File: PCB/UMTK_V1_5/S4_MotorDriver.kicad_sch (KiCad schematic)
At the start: 0 parts

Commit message: Put in Files for V1
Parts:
- added C1: CAP 1uF 6.3V 1206(3216), CAPC1206(3216)130_M, symbol UMTK-altium-import:root_1_CAP_0
- added C2: CAP 1uF 25V 1206(3216), CAPC1206(3216)130_M, symbol UMTK-altium-import:root_0_CAP_0
- added C3: CAP 47nF 50V 1206(3216), CAPC1206(3216)130_L, symbol UMTK-altium-import:root_1_CAP_0
- added C4: 0.1u, Ceramic Cap 5mm, symbol UMTK-altium-import:root_0_Cap
- added J2: Motor Out, symbol Connector:Screw_Terminal_01x02
- added J3: Motor Shunt, symbol Connector:Screw_Terminal_01x02
- added R25: Res1, AXIAL-0.3-3D, symbol UMTK-altium-import:root_0_Res1
- added R26, R27, R32: Res1, AXIAL-0.3-3D, symbol UMTK-altium-import:root_2_Res1
- added R28, R29, R30: Res1, AXIAL-0.3-3D, symbol UMTK-altium-import:root_1_Res1
- added R31: Res1, AXIAL-0.3-3D, symbol UMTK-altium-import:root_3_Res1
- added X3: DRV8873H, DRV8873, symbol UMTK-altium-import:root_0_DRV8873
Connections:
- new net: R31.1, R32.2, X3.10 (IPROPI1), X3.12 (IPROPI2)
- new net: R26.1, R27.1, X3.4 (SR)
- new net: C1.2, X3.1 (DVDD)
- new net: C2.2, X3.21 (VCP)
- new net: C3.1, X3.23 (CPL)
- new net: C3.2, X3.22 (CPH)
- new net +12V: J3.1 (Pin_1)
- new net +5: R25.1, R26.2, R28.2, R29.2, R30.2, X3.3 (MODE)
- new net GND: C1.1, C4.2, R27.2, R31.2, X3.16 (SRC), X3.17 (SRC), X3.24 (GND), X3.25 (PPAD)
- new net M_DISABLE: R30.1, X3.2 (nFAULT)
- new net M_EN/IN1: X3.7 (EN/IN1)
- new net M_FAULT: X3.9 (DISABLE)
- new net M_ISENS: C4.1, R32.1
- new net M_ITRIP: R29.1, X3.5 (nITRIP)
- new net M_OL: R28.1, X3.6 (nOL)
- new net M_PH/IN2: X3.8 (PH/IN2)
- new net M_SLEEP: R25.2, X3.11 (nSLEEP)
- new net VM+: J2.2 (Pin_2), X3.18 (OUT2), X3.19 (OUT1)
- new net VM-: J2.1 (Pin_1), X3.14 (OUT2), X3.15 (OUT2)
- new net Vmot: C2.1, X3.13 (VM), X3.20 (VM)
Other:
- note added: "Motor Connections"
- note added: "Motor Driver (DRV8873)"

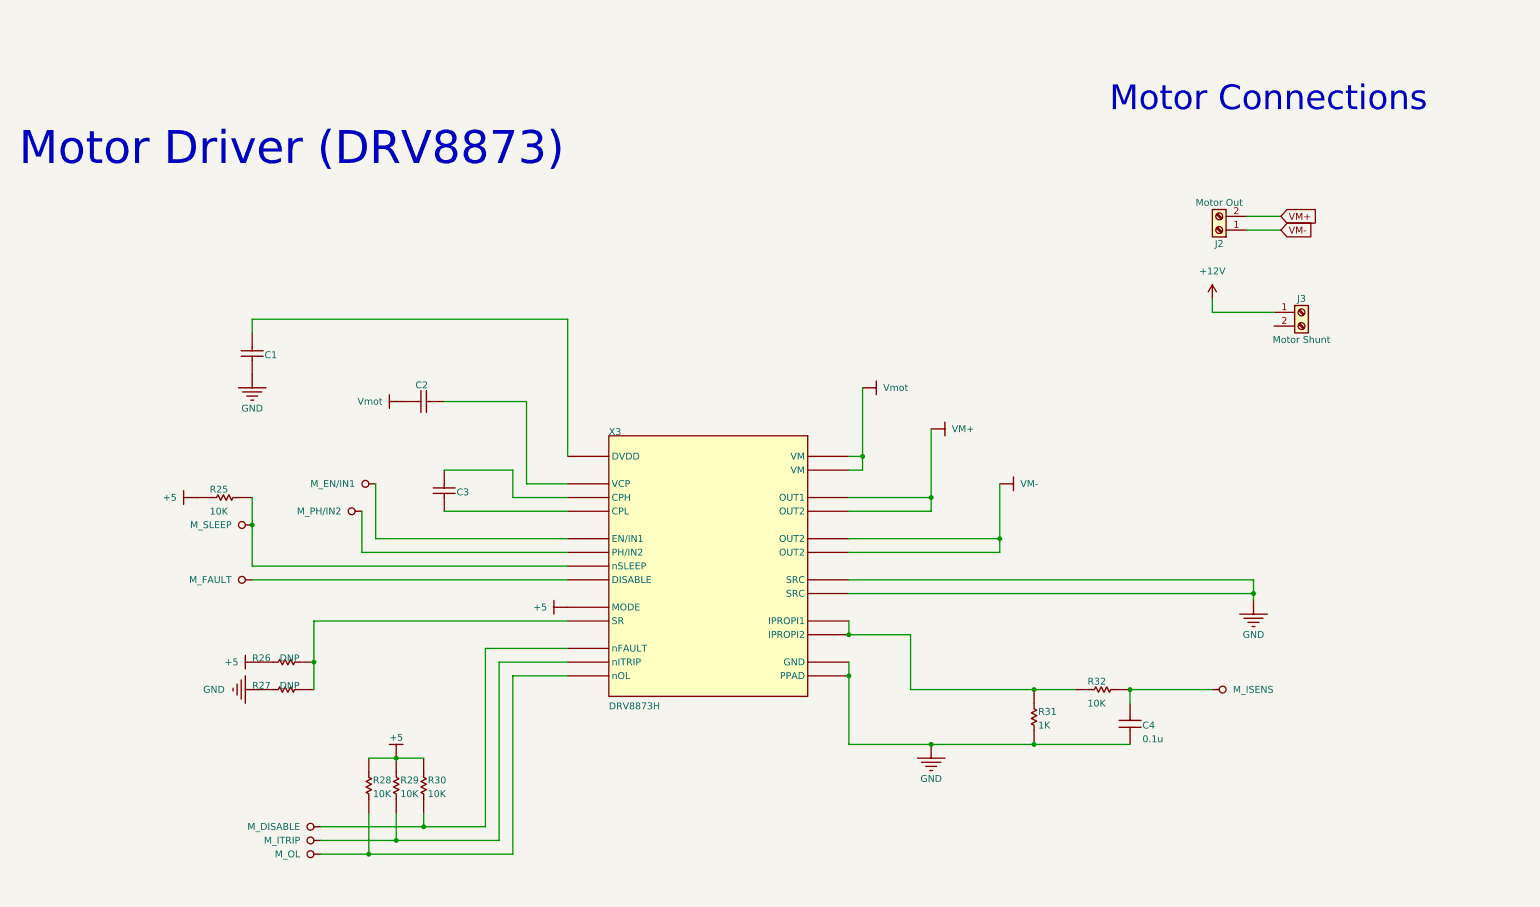
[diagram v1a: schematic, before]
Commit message: Updated Schematics
Done: 7 Seg, Power, Motor, Slide, HX711
To Do: Arduino
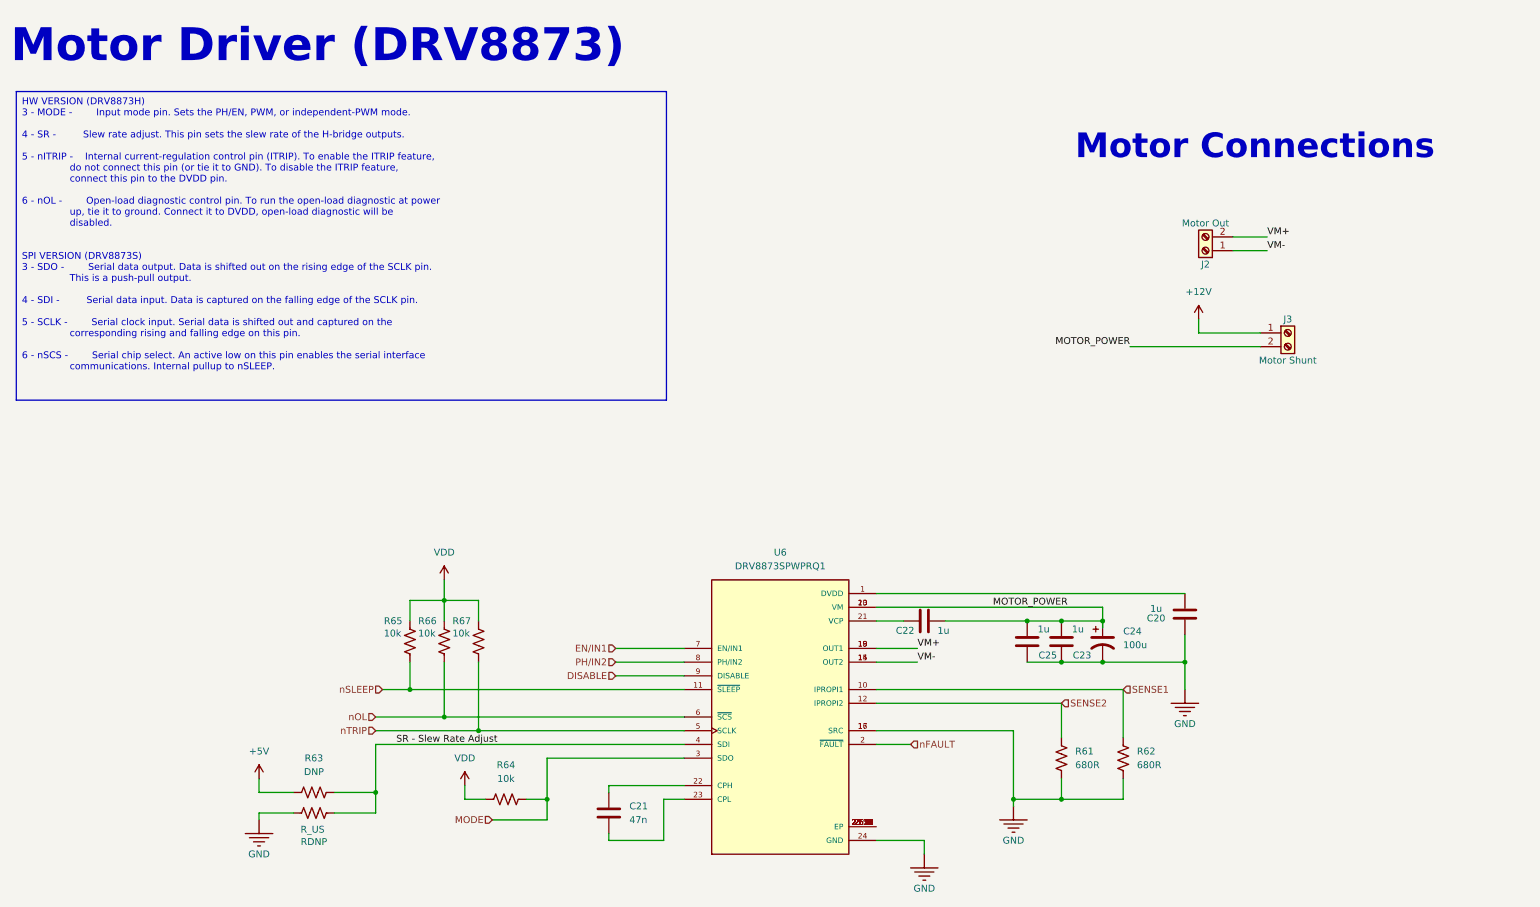
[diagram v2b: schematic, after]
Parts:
- removed C1: CAP 1uF 6.3V 1206(3216), CAPC1206(3216)130_M, symbol UMTK-altium-import:root_1_CAP_0
- removed C2: CAP 1uF 25V 1206(3216), CAPC1206(3216)130_M, symbol UMTK-altium-import:root_0_CAP_0
- removed C3: CAP 47nF 50V 1206(3216), CAPC1206(3216)130_L, symbol UMTK-altium-import:root_1_CAP_0
- removed C4: 0.1u, Ceramic Cap 5mm, symbol UMTK-altium-import:root_0_Cap
- removed R25: Res1, AXIAL-0.3-3D, symbol UMTK-altium-import:root_0_Res1
- removed R26, R27, R32: Res1, AXIAL-0.3-3D, symbol UMTK-altium-import:root_2_Res1
- removed R28, R29, R30: Res1, AXIAL-0.3-3D, symbol UMTK-altium-import:root_1_Res1
- removed R31: Res1, AXIAL-0.3-3D, symbol UMTK-altium-import:root_3_Res1
- removed X3: DRV8873H, DRV8873, symbol UMTK-altium-import:root_0_DRV8873
- added C20, C22, C23, C25: 1u, symbol Device:C
- added C21: 47n, symbol Device:C
- added C24: 100u, symbol Device:C_Polarized_US
- added R61, R62: 680R, symbol Device:R_US
- added R63: DNP, symbol Device:R_US
- added R64, R65, R66, R67: 10k, symbol Device:R_US
- added RDNP: R_US, symbol Device:R_US
- added U6: DRV8873SPWPRQ1, DRV8873SPWPRQ1:IC_DRV8873SPWPRQ1, symbol DRV8873SPWPRQ1:DRV8873SPWPRQ1
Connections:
- net GND: now also C20.2, C23.1, C24.2, C25.1, R61.1, R62.1, RDNP.1, U6.16 (SRC), U6.17 (SRC), U6.24 (GND)
- net VM+: now also U6.18 (OUT1), U6.19 (OUT1)
- net VM-: now also U6.14 (OUT2), U6.15 (OUT2)
- net MOTOR_POWER: now reaches J3.2 (Pin_2)
- net MOTOR_POWER: now also C22.2, C23.2, C24.1, C25.2, U6.13 (VM), U6.20 (VM)
- new net: C20.1, U6.1 (DVDD)
- new net: C22.1, U6.21 (VCP)
- new net: C21.1, U6.22 (CPH)
- new net: C21.2, U6.23 (CPL)
- new net: U6.25 (EP), U6.25.1 (EP), U6.25.10 (EP), U6.25.11 (EP), U6.25.12 (EP), U6.25.13 (EP), U6.25.14 (EP), U6.25.15 (EP), U6.25.16 (EP), U6.25.17 (EP), U6.25.18 (EP), U6.25.2 (EP), U6.25.3 (EP), U6.25.4 (EP), U6.25.5 (EP), U6.25.6 (EP), U6.25.7 (EP), U6.25.8 (EP), U6.25.9 (EP)
- new net +5V: R63.2
- new net DISABLE: U6.9 (DISABLE)
- new net EN/IN1: U6.7 (EN/IN1)
- new net MODE: R64.2, U6.3 (SDO)
- new net PH/IN2: U6.8 (PH/IN2)
- new net SENSE1: R62.2, U6.10 (IPROPI1)
- new net SENSE2: R61.2, U6.12 (IPROPI2)
- new net SR - Slew Rate Adjust: R63.1, RDNP.2, U6.4 (SDI)
- new net VDD: R64.1, R65.2, R66.2, R67.2
- new net nFAULT: U6.2 (~{FAULT})
- new net nOL: R66.1, U6.6 (~{SCS})
- new net nSLEEP: R65.1, U6.11 (~{SLEEP})
- new net nTRIP: R67.1, U6.5 (SCLK)
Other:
- moved on the sheet: J2, J3

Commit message: Updating Schematic
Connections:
- net MOTOR_POWER renamed VMOTOR
- net nTRIP renamed nITRIP
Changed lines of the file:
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@@
+	)
+	(junction
+		(at 215.9 120.65)
+		(diameter 0)
+		(color 0 0 0 0)
 	)
 	(junction
@@
 	(wire
 		(pts
+			(xy 215.9 110.49) (xy 215.9 120.65)
+		)
+		(stroke
+			(width 0)
+			(type default)
+		)
+	)
+	(wire
+		(pts
 			(xy 113.03 156.21) (xy 113.03 148.59)
 		)
@@
 		)
 	)
-	(label "MOTOR_POWER"
+	(global_label "VMOTOR"
+		(shape input)
 		(at 220.98 72.39 180)
 		(fields_autoplaced yes)
@@
 				(size 1.27 1.27)
 			)
-			(justify right bottom)
+			(justify right)
+		)
+		(property "Intersheetrefs" "${INTERSHEET_REFS}"
+			(at 210.5562 72.39 0)
+			(effects
+				(font
+					(size 1.27 1.27)
+				)
+				(justify right)
+				(hide yes)
+			)
+		)
+	)
+	(global_label "VMOTOR"
+		(shape input)
+		(at 215.9 110.49 180)
+		(fields_autoplaced yes)
+		(effects
+			(font
+				(size 1.27 1.27)
+			)
+			(justify right)
+		)
+		(property "Intersheetrefs" "${INTERSHEET_REFS}"
+			(at 205.4762 110.49 0)
+			(effects
+				(font
+					(size 1.27 1.27)
+				)
+				(justify right)
+				(hide yes)
+			)
 		)
 	)
@@
 		)
 	)
-	(hierarchical_label "nTRIP"
+	(hierarchical_label "nITRIP"
 		(shape input)
 		(at 81.28 143.51 180)
